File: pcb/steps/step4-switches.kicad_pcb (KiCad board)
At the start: 2 copper layers, 98 x 50 mm, 35 parts, among them SW1 ChocV2, SW10 ChocV2, SW11 ChocV2, SW12 ChocV2, SW13 ChocV2, SW14 ChocV2, SW2 ChocV2, SW3 ChocV2, SW4 ChocV2, SW5 ChocV2, SW6 ChocV2, SW7 ChocV2, SW8 ChocV2, SW9 ChocV2

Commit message: 第二版渲染层同步：3D 模型 12→13 脚、主控 USB 朝向、参考图数据更新
改板后「展示层」全部重生成 —— 否则它们会自信地展示错误信息（本项目的老教训）。

- tools/gen_step_models.py：
  · header_pins_front 12 根 → **13 根**（跨距 30.48）
  · header_plastic_back 胶条 27.94 → **30.48**（中心 13.97 → 15.24）
  · promicro_at_JP1 挂载偏移 13.97 → **15.24**（13 孔跨距的中点，原值是按 12 孔算的）
  · USB-C 从「+x（右壁）」改成「-y（短边，pad1 端）」—— 原模型朝错方向
- tools/render_assembly.py：JP_N 12→13、JP_Y0 15.03→15.26、NANO 本体 y[12.50,45.50]
  → y[14.00,47.00]（这三处是写死的副本，不改就会画出旧板子）
- 重生成产物：cad/models/*.step、docs/img/step0~5*.png（8 张）、
  pcb/steps/*.kicad_pcb（6 个变体）、docs/img/焊接参考-*.svg、docs/焊接参考图.html
- 新增 docs/img/pcb-v2-{front,back}.png：kicad-cli pcb render 直接渲染的裸板
  （数据源就是 pcb/claudepad.kicad_pcb 本身，不存在副本漂移）

校验：渲染图中排针两列各 13 根、跨距 30.48；背面主控 USB-C 已朝短边
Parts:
- JP1, JP2: footprint PinHeader_1x12_P2.54mm_Vertical -> PinHeader_1x13_P2.54mm_Vertical
- moved JP1 2.77 mm to (81.0, 4.26)
- moved JP2 2.77 mm to (96.2, 4.26)
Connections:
- JP1 pad 1: (no net) -> GND
- JP1 pad 10: COL1 -> ROW3
- JP1 pad 11: COL2 -> COL1
- JP1 pad 12: COL3 -> COL2
- JP1 pad 3: GND -> (no net)
- JP1 pad 5: (no net) -> GND
- JP1 pad 7: ROW1 -> (no net)
- JP1 pad 8: ROW2 -> ROW1
- JP1 pad 9: ROW3 -> ROW2
- JP2 pad 10: COL6 -> RGB_DIN
- JP2 pad 11: COL5 -> COL6
- JP2 pad 12: COL4 -> COL5
- JP2 pad 2: GND -> (no net)
- JP2 pad 3: RST -> GND
- JP2 pad 4: (no net) -> RST
- JP2 pad 9: RGB_DIN -> (no net)
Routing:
- net ROW1: track 148.3 -> 0.00 mm
- net COL1: track 142.1 -> 0.00 mm
- net ROW2: track 137.4 -> 0.00 mm
- net ROW3: track 128.4 -> 0.00 mm
- net COL2: track 93.4 -> 0.00 mm
- net COL3: track 91.5 -> 0.00 mm
- net COL4: track 81.8 -> 0.00 mm
- net COL5: track 75.3 -> 0.00 mm
- net GND: track 38.4 -> 0.00 mm
- net RST: track 38.2 -> 0.00 mm, vias 2 -> 0
- net COL6: track 26.8 -> 0.00 mm
- net RGB_DIN: track 20.9 -> 0.00 mm
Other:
- board text added: "USB -> +Y WALL (top)"
- board text removed: "USB -> RIGHT WALL"

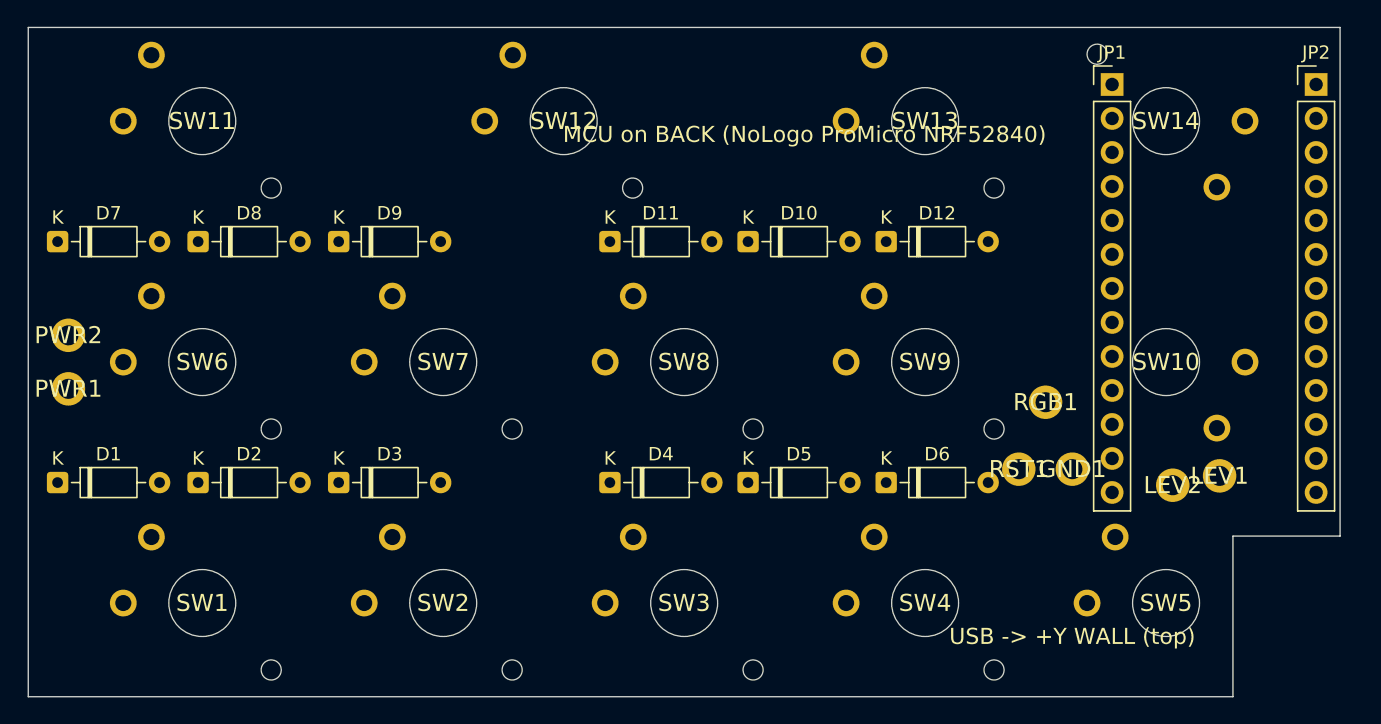
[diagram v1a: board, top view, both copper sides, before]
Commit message: ★ 14 颗轴体全部补齐 4 孔：板宽 98→99 + 主控位置重新解算
承接上一笔：上一笔判定「回车(2) 的定位脚几何无解，装配时剪脚」。用户提出
「让两条腿和另一条腿分居排针两侧」——顺着这个思路重算，发现不是无解，
只差 0.9mm，而这点位移可以靠**加宽板子 1mm** 换出来。

改动
- PCB_W 98 → 99，PCB_X 写死 2.0（不再按居中算：定位板轴孔在板坐标 15/33/…/87，
  PCB 轴体在 13/31/…/85，必须 PCB_X + 13 = 15。PCB_X 一变整机就装不上）
- PCB_NOTCH_D 8 → 9（板加宽后同步 +1，使缺口内缘**绝对位置不变**，仍在板坐标 x=90）
- 主控位置**解出来的**（穷举 0.01mm 步长取最小余量最大者）：
  NANO_POS_X 79.70→80.11、NANO_POS_Y 14.00→12.26
  左排孔 80.97→81.38、右排 96.21→96.62、pad1 y 45.74→44.00
  四条约束（回车(2)定位脚≥1.85、回车(2)中心孔≥3.60、语音中心孔≥3.60、
  语音定位脚≥1.85，均按「孔边缘↔对方铜皮」算）最小余量 **0.119mm** ✓
  ⚠️ 关键点：2.54 的孔栅格必须与 25.0/43.0 两个 Ø5 中心孔错开半格，
  否则最近孔正对中心孔，怎么挪 x 都不够
- NPTH_SKIP 清空 → **14 颗轴体 × 4 孔 = 56 孔，一条腿都不用剪**
- 焊接指南：删掉「回车第2轴剪定位脚」（已不成立），保留「轴体先焊、主控最后装」

顺带修掉两处**重复计算**（同一类 bug，都是「量恰好相等时看不出来」）
- tools/gen_pcb.py：自己又算了一遍 (PLATE_W−PCB_W)/2 而不读 params 的 PCB_X
  → 板加宽后 1.5 vs 2.0 分叉，所有轴体 PCB 坐标整体漂 0.5mm
- tools/check_dims.py：同一处重复计算 → 误报「支撑台不在间隙中心」
  两处都改为只读 params

校验：DRC 0 错误（56 个轴体孔全部保留）；check_dims 29/29、lint_scad、verify_geometry、
check_keymap、export_stl、verify_stl、gen_viewer、draw_travel、test_hook 全过；
渲染层（步骤图/参考图/裸板渲染）全部重生成
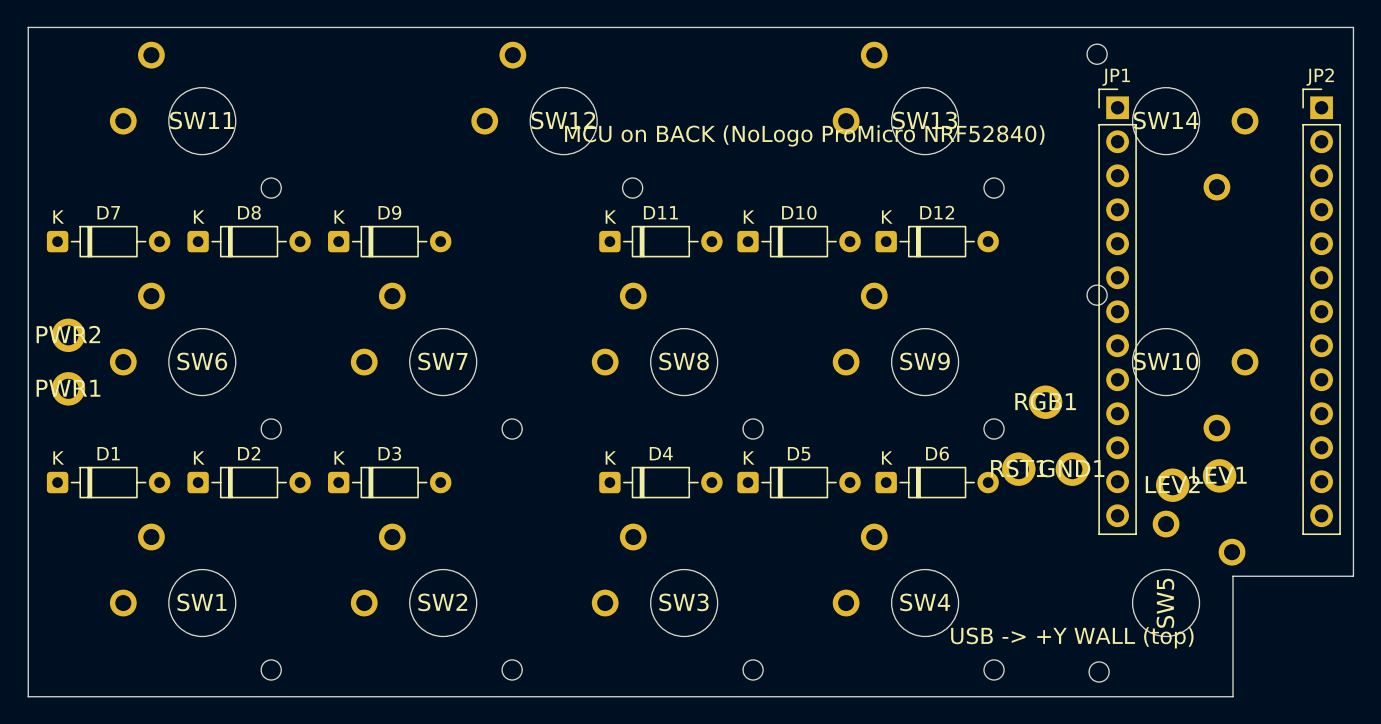
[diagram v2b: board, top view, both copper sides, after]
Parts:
- moved JP2 1.79 mm to (96.6, 6.00)
- moved JP1 1.79 mm to (81.4, 6.00)
- turned SW5 to -90 degrees
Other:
- board size 98 x 50 mm -> 99 x 50 mm

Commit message: 布局改版：空格跨列 1-4 → 2-4（3u）+ 回车(2) 转 90° 孔竖着 + 主控重新解算
按用户要求改的三件事：

【1】空格那一行紧凑对齐
  KEYMAP 的 [1,3,4,SPACE] → [2,3,3,SPACE]。3 根轴从 13/40/67（间距 27）变成
  31/49/67（间距 18），与上面两行的列对齐，行内不再有大空档，最左一列空出。
  连带：键帽 4u(71.6mm) → 3u(53.6mm)；keycap.scad 的 keycap_mode 增加 3u、去掉 4u；
  export_stl 输出 05_keycap_3u.stl（旧的 4u STL 已删）

【2】回车(2) 转 90°，孔竖着
  SWITCH_ROT 的 (ENTER,1) 由 180 改 90。它的定位脚随之落到 (90.00,30.15)、
  电气脚落到 (80.07,21.20) —— 后者要求主控左排孔从 81.38 挪到 78.03，
  而左移会被 x=76 的支撑台挡住 → 支撑台 X2 由 76 改到 58（同为列间隙中心）
  主控左移后压住复位/RGB 三个飞线焊盘 → PAD_GND (78,17)→(74,13)、
  PAD_D15 (76,22)→(75.5,22)

【3】主控位置重新解算（不是手调）
  把 14 颗轴体 56 个孔 + 支撑台 + 板缘 + 缺口一起列为约束，穷举 0.01mm：
  左排 78.03 / 右排 93.27 / pad1 y=45.30，主控本体 x[76.76,94.54] y[13.56,46.56]
  最小余量 0.682mm（比上一版的 0.119mm 宽裕得多）
  注：排针孔按「孔边缘 ↔ 对方铜皮」算，且 pad1 是方盘（有效半径 1.20 不是 0.85）

校验：DRC 0 错误；check_dims 29/29、lint_scad、verify_geometry、check_keymap、
verify_stl、export_stl、gen_viewer、draw_travel、test_hook 全过

修掉四处会撒谎的展示层（都是 4u 空格时代的硬拷贝）
- tools/verify_stl.py：期望清单还写着 05_keycap_4u.stl，而它只遍历目录里实际存在的
  文件，所以改名后静默跳过、照样报「全部通过」。已改为 3u 并新增反向检查（清单里的
  文件必须都在）；用改名做了变异测试，确认它现在真的会报错
- tools/view_model.py、cad/output/viewer.html(CAP_FILES)、cad/pcb_assembly.scad、
  tools/render_assembly.py：写死的旧空格坐标(13/40/67)与旧文件名
- tools/render_assembly.py：删掉「STOP、ENTER 第二轴没有定位孔属正常」这句（已不成立）
- 新增 docs/img/board-annotated.png（带标注对照图）
      docs/img/space-row-before-after.png（空格改前/改后示意）
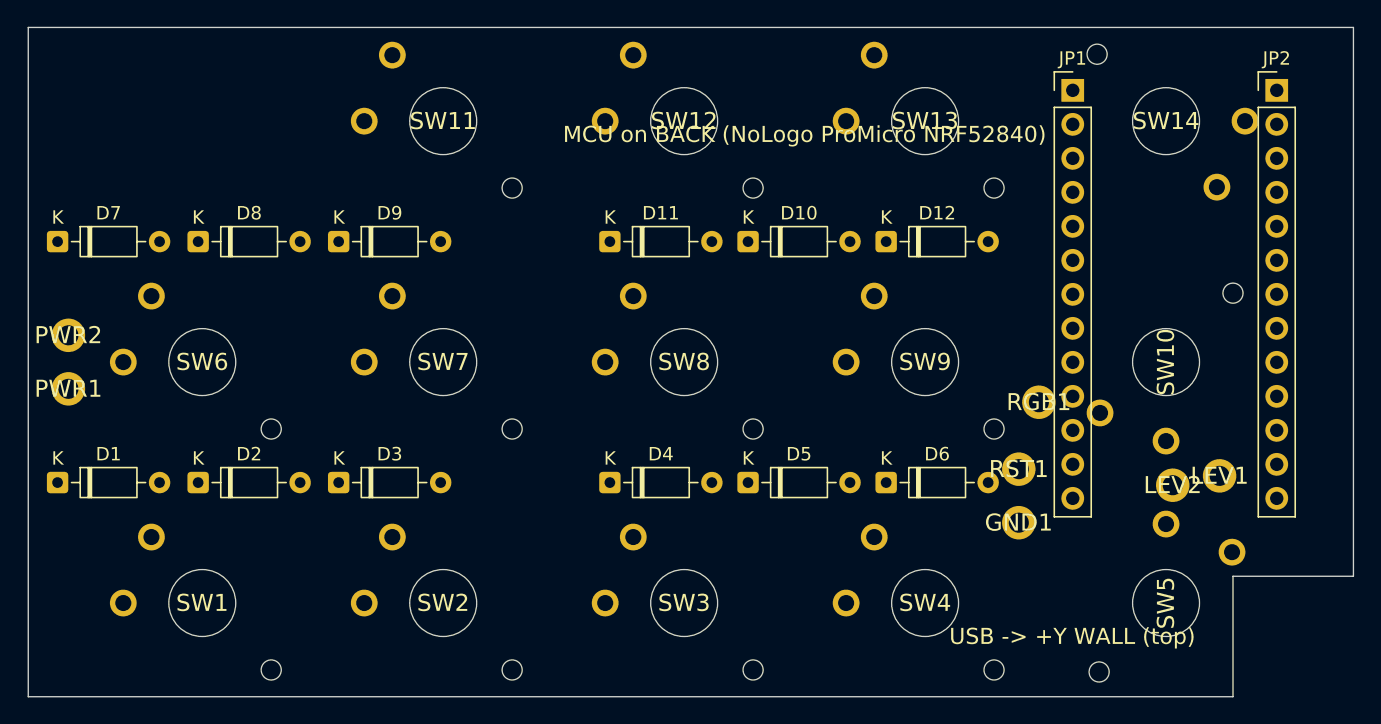
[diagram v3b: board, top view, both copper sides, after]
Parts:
- moved SW11 18.0 mm to (31.0, 7.00)
- moved SW12 9.00 mm to (49.0, 7.00)
- moved GND1 5.66 mm to (74.0, 37.0)
- moved JP2 3.59 mm to (93.3, 4.70)
- moved JP1 3.59 mm to (78.0, 4.70)
- moved RGB1 0.50 mm to (75.5, 28.0)
- turned SW10 to 90 degrees
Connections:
- D11 pad 2: COL1 -> COL2
- SW11 pad 1: COL1 -> COL2
- SW12 pad 1: COL1 -> COL2
- SW13 pad 1: COL1 -> COL2

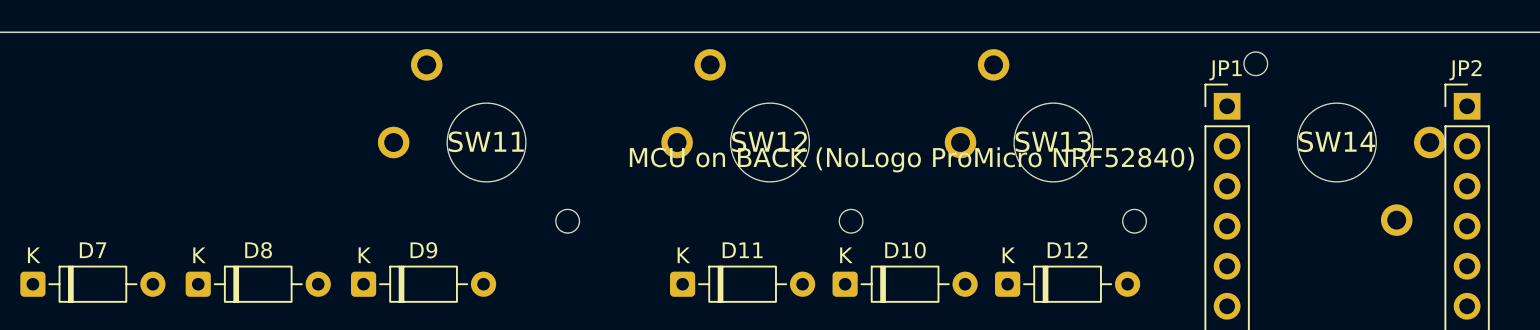
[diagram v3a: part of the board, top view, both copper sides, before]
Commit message: 布局再改：空格那行 4 颗键贴左排（跨列 1-3 + 语音列 4）+ 定位板切孔 bug 修复
用户原话（2026-10-11）：'最下层不是有四个键而已吗？我们之间给他并排与上方对其'
+ 澄清 '第 1~4 列，最左列不该空出来'。上一版误改成跨列 2-4 + 最左列空出，方向反了。

【1】空格行贴左
  KEYMAP [2,3,3,SPACE] + [5,3,1,VOICE] → [1,3,3,SPACE] + [4,3,1,VOICE]
  空格 3 轴 31/49/67 → 13/31/49（全部落在 18mm 网格线上）；语音键列 5 → 列 4
  列 5（x=85）空出 → 主控上方不再压任何轴体（原 VOICE 正好压在主控上）
  连带：overlay 矩阵变换末行 RC(2,4) → RC(2,3)；空格 net COL2 → COL1

【2】★ 定位板切孔 bug（渲染预览时发现）
  choc_cutout() 用 linear_extrude(center=true) 又被 translate z=-1，
  切槽只覆盖 z[-2.6,0.6]，而板厚 [0,1.2] → 顶面留 0.6mm 皮没切穿。
  STL 体积 6.33 cm³（实心板 + 4 螺丝孔）→ 修后 4.61 cm³。
  也就是说：**之前导出的定位板 STL 轴体根本插不进去**。

【3】展示层修漂移（都是会撒谎的硬拷贝）
  · tools/render_assembly.py：写死的板宽 98 / JP 80.97 / NANO 79.70 / 空格 31-49-67
    → 全改为读 pcb/placement.csv + 板文件 + params；俯视图孔位改为按真实旋转角算
    （原先只做 180° 镜像，STOP 270° / ENTER 90° 的孔画错位置）
  · cad/pcb_assembly.scad：SWITCHES / JP_XS / JP_N / 主控位置与 USB 朝向 / 复位焊盘
  · tools/check_dims.py：空格挠度按 4u 算 → 从 KEYMAP 推导（3u：单轴 0.67 / 三轴 0.08）
  · 新增 tools/render_board_annotated.py：board-annotated.png 等改由脚本生成

【4】重生成产物
  pcb/claudepad.kicad_pcb（99×50）· pcb/steps/*（6 个）· placement.csv / netlist / wiring
  cad/output/*.stl（6 个，含修好的定位板）· docs/img/*（板子 5 视角 + 分步 8 张 +
  焊接参考图 + 标注图 + 顶视预览）· pcb/claudepad_render.kicad_pcb（含 3D 模型）

【5】文档同步：焊接指南 / PCB 规格书 / 打样下单指南 / 改板方案 / PRD / 结构 / 采购 /
  项目报告 / README / firmware README / MEMORY.md（4u→3u、98→99、排针列位、主控坐标）

校验：check_dims 29/29 · lint_scad · verify_geometry · check_keymap · verify_stl ·
test_hook 全过；DRC 0 错误（39 条丝印警告 + 59 未连接，未布线预期）
⚠️ 尚未布线、未出 Gerber（打样前必须补）
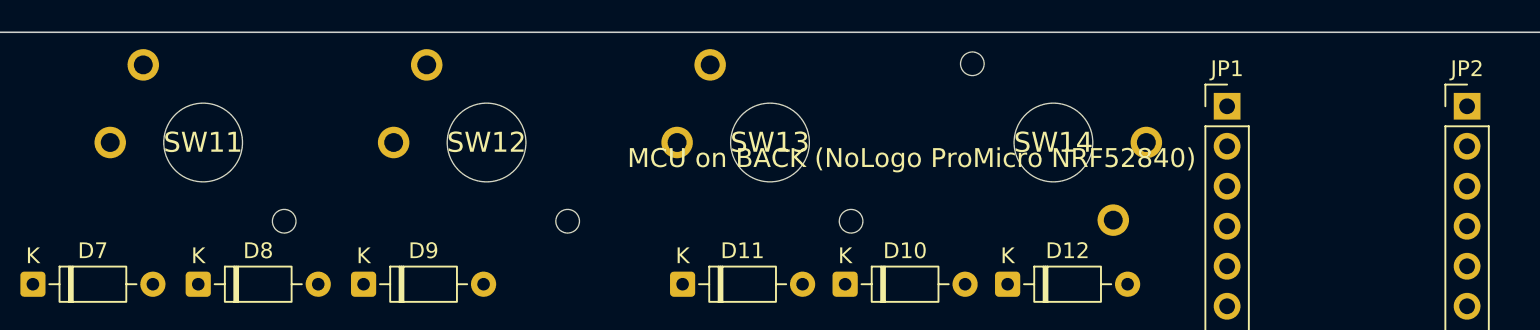
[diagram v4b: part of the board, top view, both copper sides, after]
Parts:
- moved SW11 18.0 mm to (13.0, 7.00)
- moved SW12 18.0 mm to (31.0, 7.00)
- moved SW13 18.0 mm to (49.0, 7.00)
- moved SW14 18.0 mm to (67.0, 7.00)
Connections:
- D11 pad 2: COL2 -> COL1
- D12 pad 2: COL5 -> COL4
- SW11 pad 1: COL2 -> COL1
- SW12 pad 1: COL2 -> COL1
- SW13 pad 1: COL2 -> COL1
- SW14 pad 1: COL5 -> COL4

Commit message: 布线完成 + 修致命电路拓扑（二极管/轴体并联 → 串联）+ 出 Gerber
⚠️ 用户要求『去嘉立创下单』，但板子当时不能下单：没布线、Gerber 是第一版的。
   本次把前置条件全部做完了。

【1】★ 致命电路错误：二极管与轴体并联（发现于核对焊盘网络）
  SW1: pad1→COL1, pad2→ROW1 ／ D1: K→ROW1, A→COL1 —— 两者**并联**。
  后果：驱动任一列都会经二极管直接灌通行线 → 该列按键恒为『按下』，键盘不可用。
  正解（与 netlist.md 的『列 → 阳极 → 阴极 → 轴体 → 行』一致）是**串联**：
      列 COL ── A▷|── K ── MID ── 轴体pad1 ──[按下]── pad2 ── ROW
  · gen_pcb.py：每个矩阵位置新增局部网络 net_mid（大键多轴共用；拨杆用 APPROVE_MID）
  · gen_kicad.py：轴体 pad1→MID / pad2→ROW；二极管 K→MID / A→COL
  · gen_kicad.py 自检新增**串联断言**（几何检查查不出这类错，必须断言网络）
  · 第一版板子也带这个错（已作废，未流出）

【2】自动布线（打通链路）
  tools/export_dsn.py（新增）→ FreeRouting → tools/import_ses.py → 174 段 + 3 过孔
  · FreeRouting 原生 CLI v2.5.0 在本项目 DSN 上崩（GraalVM 序列化限制），
    改用 freerouting-1.9.0.jar + OpenJDK 21（1.7 秒布完）
  · tools/patch_route.py（新增）补自动布线漏掉的 ROW3 一段（绕开两个 Ø5 中心孔）
  · DRC：**0 错误 / 0 未连接**（39 条丝印警告为既有，不影响打样）

【3】出 Gerber（第二版打样包）
  pcb/fabrication/claudepad-jlc.zip —— 10 个文件（F/B 铜箔·阻焊·丝印 + 板框 + 钻孔 + 网表）
  第一版全套（含 9-28 的 zip）归档到 pcb/fabrication/v1-2026-09-28/，避免误下单

【4】文档
  · 打样下单指南：状态改为『可以下单』，补下单参数（建议勾飞针电测）与到货核对项
  · 焊接指南：二极管极性说明改为串联口径；★ 新增『列 ↔ 行 不导通』万用表检查
  · 全部『阳极接列、阴极接行』措辞改为『阳极朝列、阴极朝行（与轴体串联）』
  · MEMORY.md：新增布线/打样链路一节（含 FreeRouting 版本坑与镜像）

校验：check_dims 29/29 · lint_scad · verify_geometry · check_keymap · verify_stl ·
test_hook 全过；DRC 0 错误 / 0 未连接
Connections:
- D1 pad 1: ROW1 -> MID_R1C1
- D10 pad 1: ROW2 -> MID_R2C4
- D11 pad 1: ROW3 -> MID_R3C1
- D12 pad 1: ROW3 -> MID_R3C4
- D2 pad 1: ROW1 -> MID_R1C2
- D3 pad 1: ROW1 -> MID_R1C3
- D4 pad 1: ROW1 -> MID_R1C4
- D5 pad 1: ROW1 -> MID_R1C5
- D6 pad 1: ROW1 -> APPROVE_MID
- D7 pad 1: ROW2 -> MID_R2C1
- D8 pad 1: ROW2 -> MID_R2C2
- D9 pad 1: ROW2 -> MID_R2C3
- SW1 pad 1: COL1 -> MID_R1C1
- SW10 pad 1: COL4 -> MID_R2C4
- SW11 pad 1: COL1 -> MID_R3C1
- SW12 pad 1: COL1 -> MID_R3C1
- SW13 pad 1: COL1 -> MID_R3C1
- SW14 pad 1: COL4 -> MID_R3C4
- SW2 pad 1: COL2 -> MID_R1C2
- SW3 pad 1: COL3 -> MID_R1C3
- SW4 pad 1: COL4 -> MID_R1C4
- SW5 pad 1: COL5 -> MID_R1C5
- SW6 pad 1: COL1 -> MID_R2C1
- SW7 pad 1: COL2 -> MID_R2C2
- SW8 pad 1: COL3 -> MID_R2C3
- SW9 pad 1: COL4 -> MID_R2C4
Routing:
- net ROW1: track 0.00 -> 111.2 mm, vias 0 -> 1
- net ROW3: track 0.00 -> 102.0 mm
- net COL1: track 0.00 -> 101.0 mm
- net ROW2: track 0.00 -> 91.6 mm
- net COL2: track 0.00 -> 77.4 mm
- net COL3: track 0.00 -> 70.5 mm, vias 0 -> 1
- net COL4: track 0.00 -> 67.0 mm, vias 0 -> 1
- net GND: track 0.00 -> 56.9 mm
- net MID_R3C1: track 0.00 -> 52.1 mm
- net RST: track 0.00 -> 44.5 mm
- net MID_R2C4: track 0.00 -> 40.3 mm
- net MID_R1C5: track 0.00 -> 38.3 mm
- net COL5: track 0.00 -> 34.4 mm
- net APPROVE_MID: track 0.00 -> 30.0 mm
- net MID_R2C3: track 0.00 -> 23.7 mm
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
